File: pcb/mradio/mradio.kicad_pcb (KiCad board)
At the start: 2 copper layers, 150 x 75 mm, 187 parts, among them J202 Conn_01x02, J301 JX0026D21BNL, J401 MM60-52B1-E1-R650, J501 MDT420E01001, U1 STM32H745ZITx, U1001 TPS7A8500ARGRR, U301 DP83825I, U401 74AVC4T774, U402 74AVC4T774, U502 SN74LVC1T45DRL, U601 TPS54560BDDA, U701 TPS54560BDDA, U801 TPS7A8500ARGRR, Y301 DSC1525JL2A-25M00000T

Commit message: started LDO
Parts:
- moved C806 147.6 mm to (28.0, 107.0)
- moved D801 147.6 mm to (36.0, 104.3)
- moved C807 147.6 mm to (32.0, 94.5)
- moved C808 147.6 mm to (32.0, 97.0)
- moved C809 147.6 mm to (32.0, 99.5)
- moved C810 147.6 mm to (32.0, 102.0)
- moved R801 147.6 mm to (32.0, 104.5)
- moved TP801 146.8 mm to (38.8, 96.6)
- moved C804 105.0 mm to (80.2, 93.2), turned to -90 degrees
- moved C805 104.4 mm to (84.5, 91.0)
- moved C803 104.1 mm to (81.2, 90.8)
- moved C802 103.4 mm to (78.8, 93.2), turned to -90 degrees
- moved C801 103.4 mm to (77.2, 93.2), turned to -90 degrees
- moved U801 35.1 mm to (83.2, 93.9), turned to 90 degrees
- moved H401 31.0 mm to (191.1, 78.6)
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
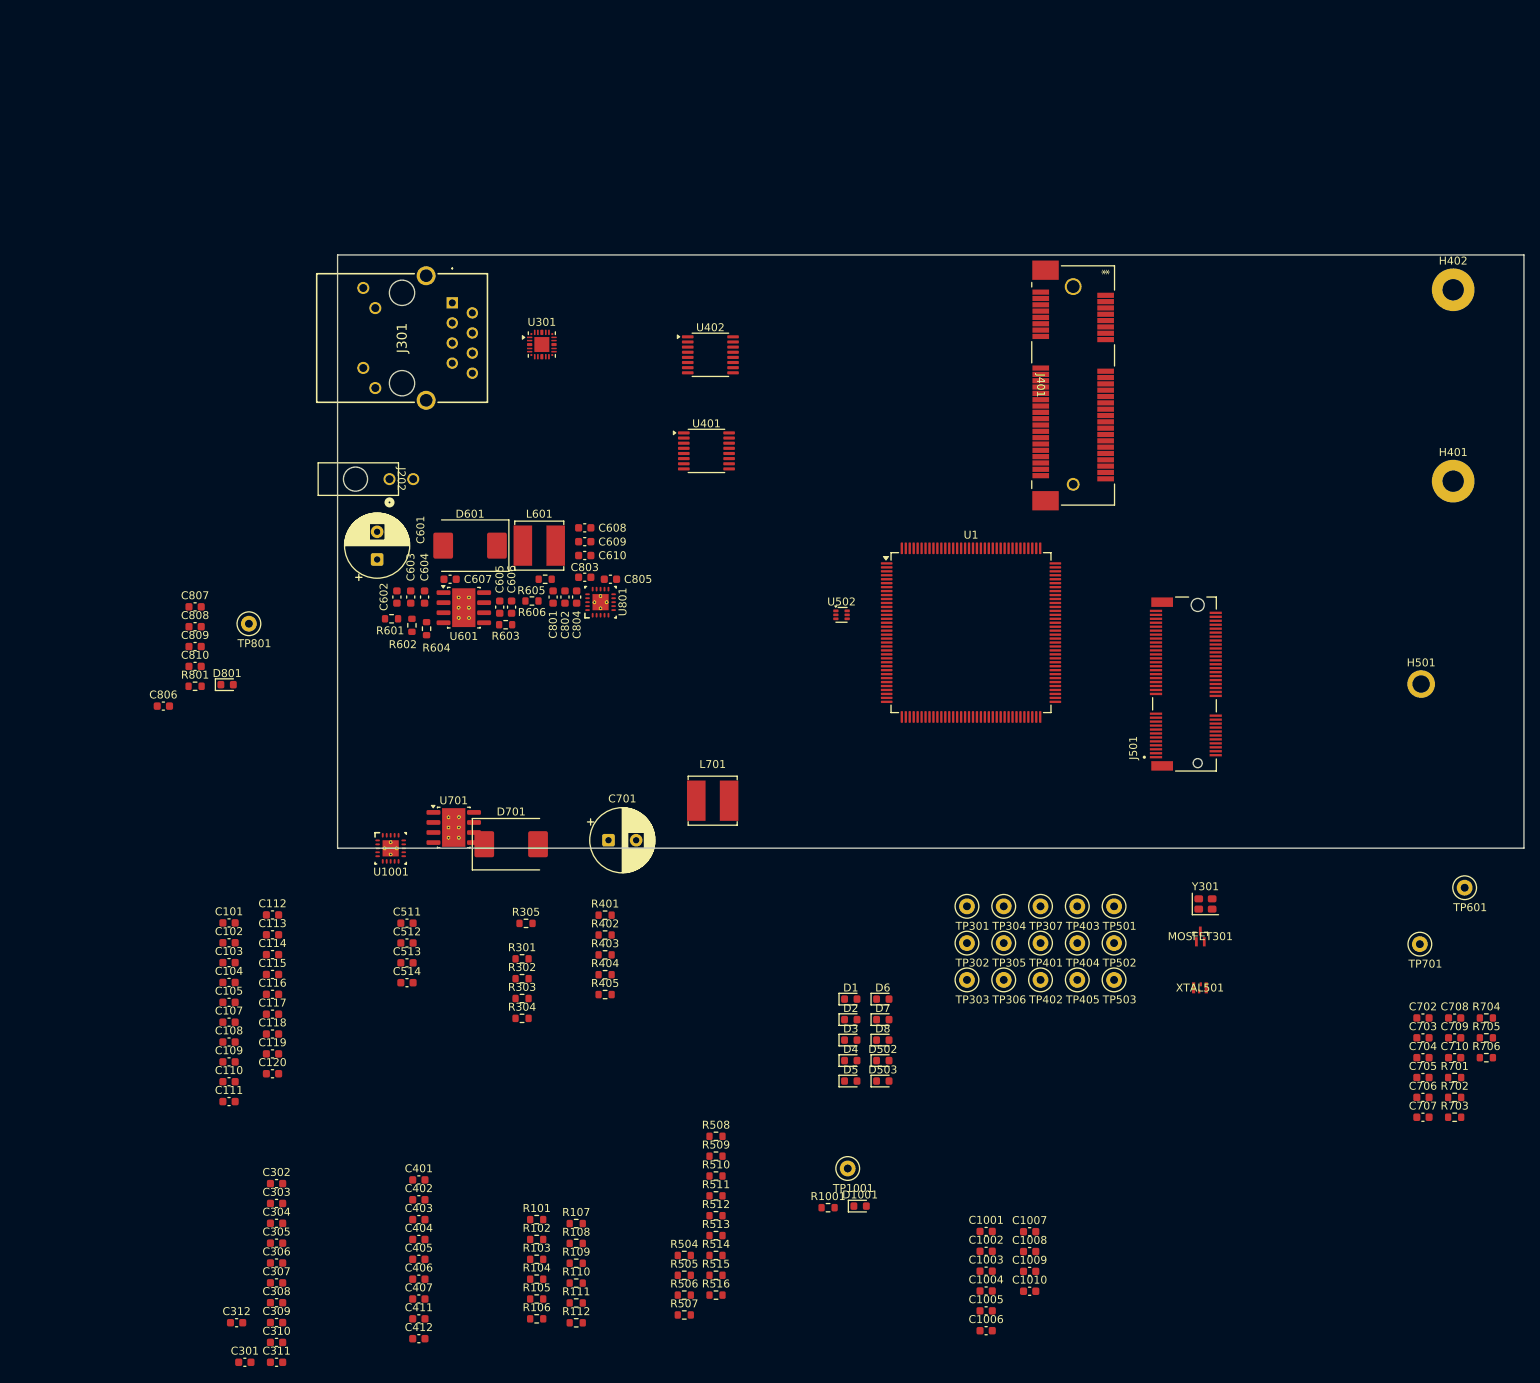
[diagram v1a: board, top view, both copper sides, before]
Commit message: Finished 12->3v3 circuit and 2v2 buck
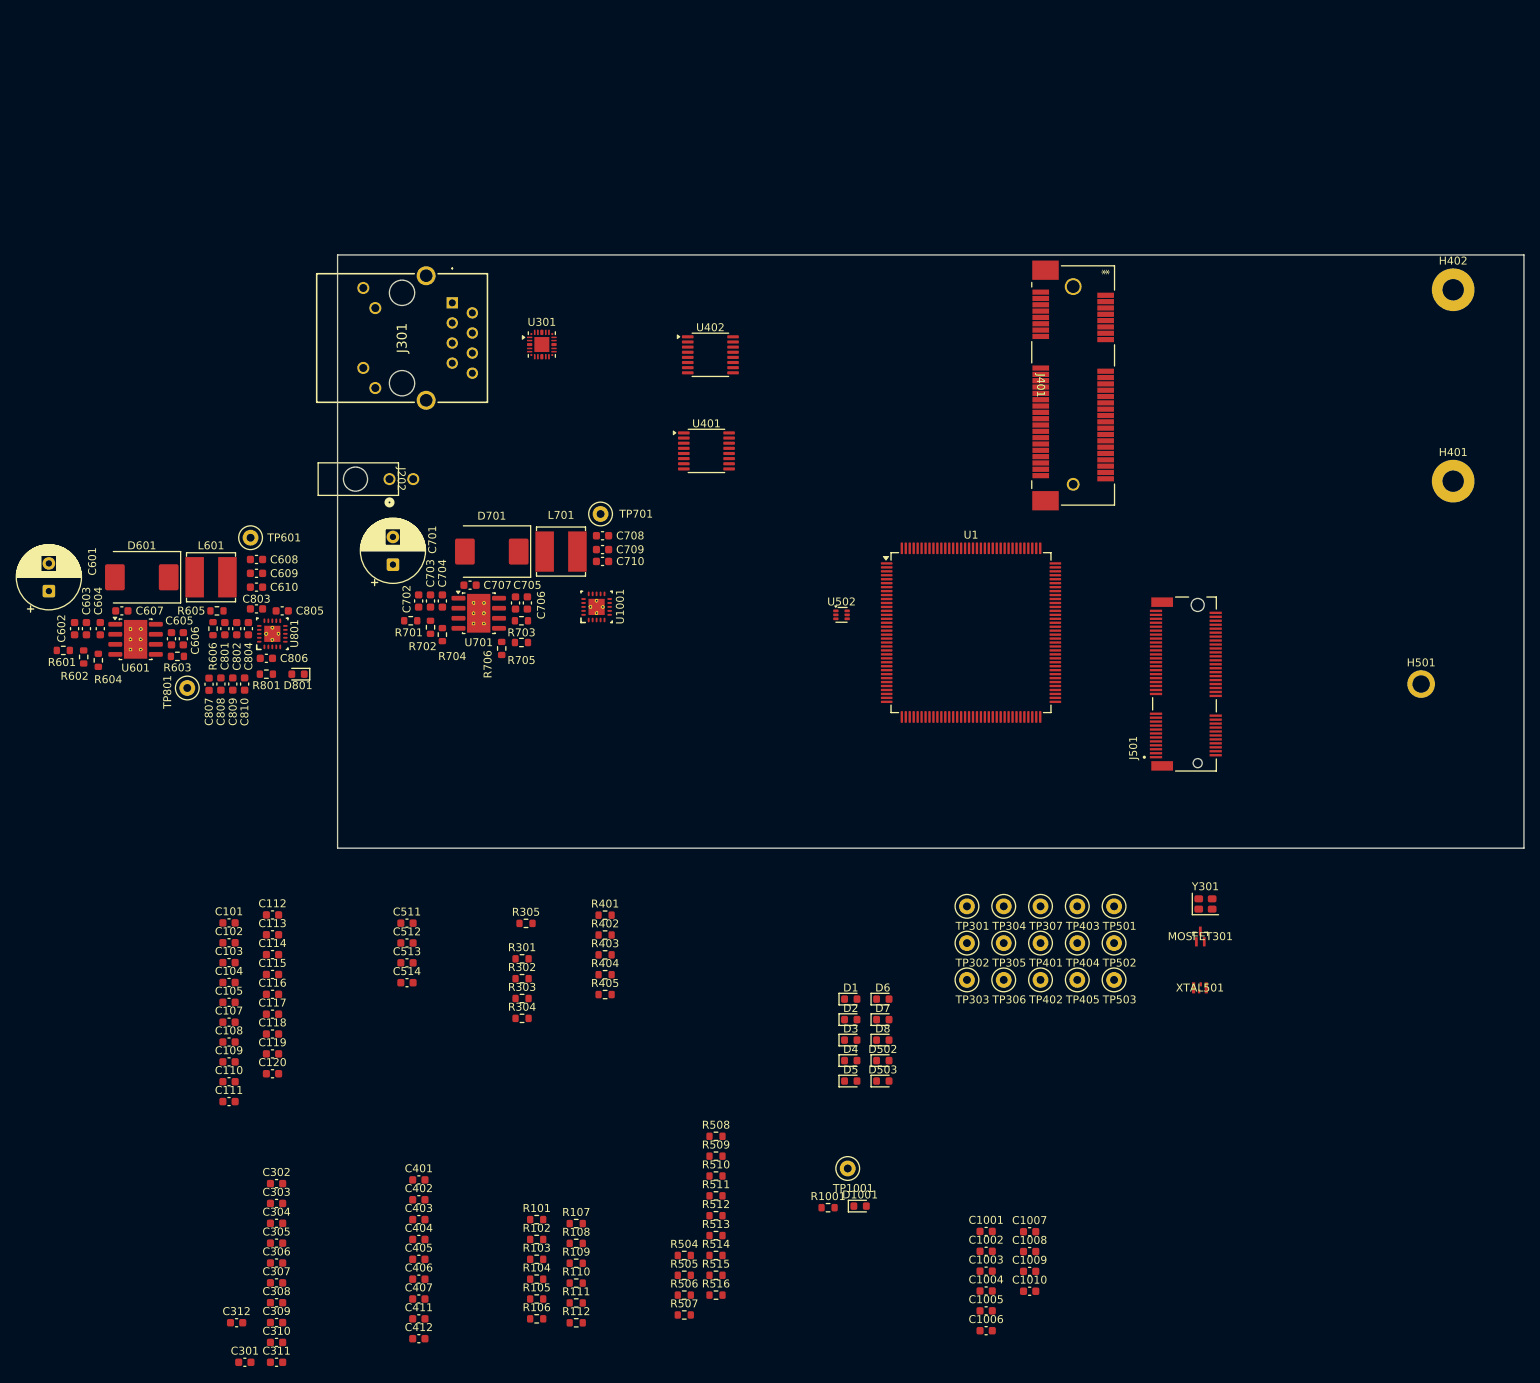
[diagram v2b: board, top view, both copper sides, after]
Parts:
- moved TP601 159.8 mm to (39.0, 85.8)
- moved R701 144.1 mm to (59.2, 96.2)
- moved R702 142.5 mm to (61.8, 97.1), turned to -90 degrees
- moved R704 140.6 mm to (63.2, 98.0), turned to -90 degrees
- moved C707 138.0 mm to (66.8, 91.8)
- moved C702 137.5 mm to (60.2, 93.8), turned to 90 degrees
- moved C703 137.1 mm to (61.8, 93.8), turned to 90 degrees
- moved C704 136.8 mm to (63.2, 93.8), turned to 90 degrees
- moved R706 134.8 mm to (70.8, 99.8), turned to -90 degrees
- moved R703 133.6 mm to (73.2, 96.2), turned to 180 degrees
- moved R705 131.8 mm to (73.2, 99.0), turned to 180 degrees
- moved C705 129.5 mm to (72.5, 94.0), turned to 90 degrees
- moved C706 129.3 mm to (74.0, 94.0), turned to 90 degrees
- moved C710 124.7 mm to (83.5, 88.8)
- moved C709 124.2 mm to (83.5, 87.2)
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
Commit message: power conversion
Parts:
- moved C910 126.6 mm to (41.0, 99.0), turned to 90 degrees
- moved C909 126.2 mm to (39.5, 99.0), turned to 90 degrees
- moved C908 125.8 mm to (38.0, 99.0), turned to 90 degrees
- moved C907 125.5 mm to (36.5, 99.0), turned to 90 degrees
- moved C905 125.2 mm to (44.8, 93.8)
- moved C904 124.5 mm to (41.0, 96.0), turned to -90 degrees
- moved C903 123.8 mm to (41.8, 93.8)
- moved C906 123.6 mm to (43.5, 99.8)
- moved C902 122.3 mm to (39.5, 96.0), turned to -90 degrees
- moved C901 121.8 mm to (38.0, 96.0), turned to -90 degrees
- moved TP901 101.2 mm to (35.2, 102.5)
- moved D901 97.1 mm to (49.2, 99.8), turned to 180 degrees
- moved R901 95.8 mm to (46.5, 100.5), turned to -90 degrees
- moved C601 47.0 mm to (60.5, 92.2)
- moved TP801 46.3 mm to (77.2, 102.5)
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- renumbered C1001 to C901, C1002 to C902, C1003 to C903, C1004 to C904, C1005 to C905, C1006 to C906, C1007 to C907, C1008 to C908, C1009 to C909, C1010 to C910, D1001 to D901, R1001 to R901, TP1001 to TP901, U1001 to U901

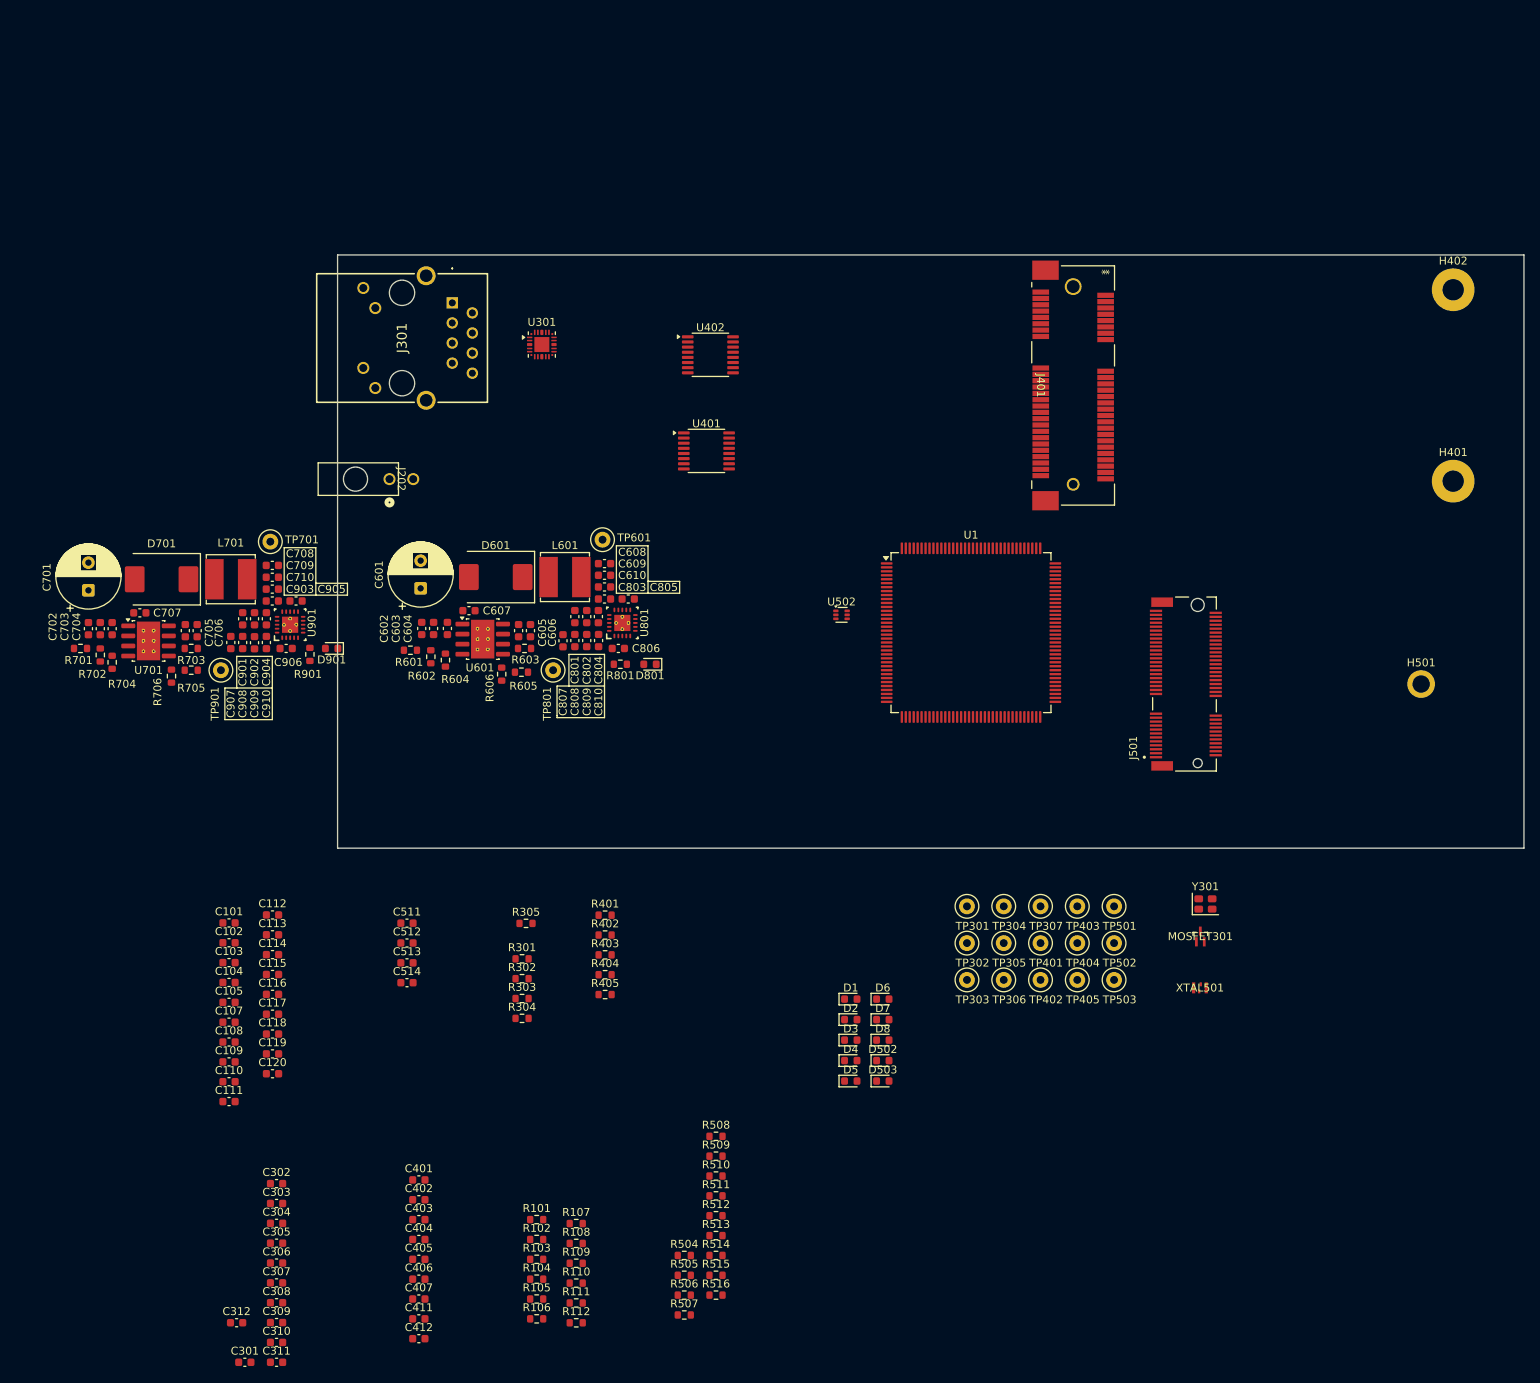
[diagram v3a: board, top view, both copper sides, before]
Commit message: SDIO class and WiFi/mag jack layout
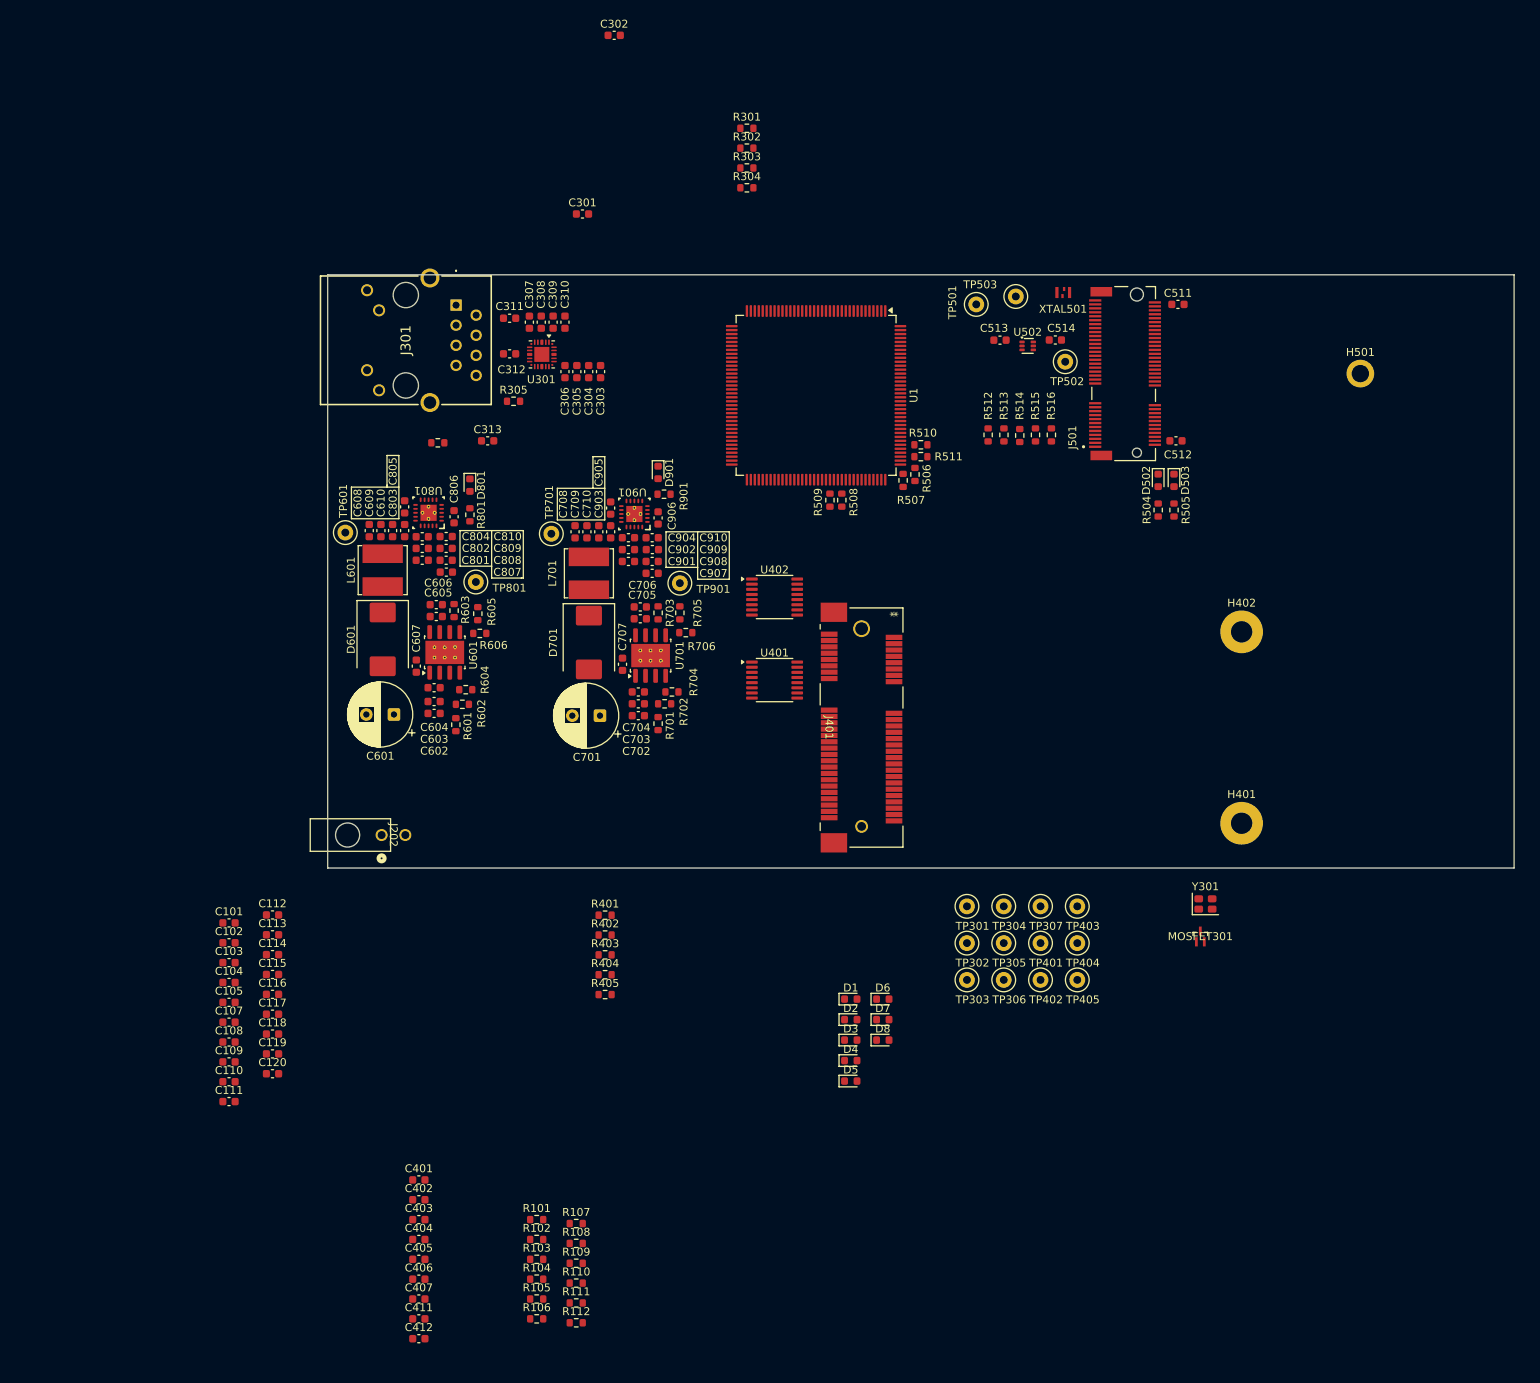
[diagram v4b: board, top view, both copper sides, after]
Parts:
- added C313: 1nF, 1KV, Capacitor_SMD:C_0603_1608Metric, F.Cu at (69.0, 73.5)
- added R306: 1M, Resistor_SMD:R_0603_1608Metric, F.Cu at (62.7, 73.8)
- moved C301 151.3 mm to (81.0, 44.8)
- moved C302 151.3 mm to (85.0, 22.2)
- moved C311 135.2 mm to (71.8, 58.0), turned to 180 degrees
- moved C310 134.0 mm to (78.8, 58.5), turned to -90 degrees
- moved C309 131.2 mm to (77.2, 58.5), turned to -90 degrees
- moved C308 128.4 mm to (75.8, 58.5), turned to -90 degrees
- moved C312 127.3 mm to (71.8, 62.5), turned to 180 degrees
- moved C307 125.6 mm to (74.2, 58.5), turned to -90 degrees
- moved C511 125.0 mm to (156.2, 56.2)
- moved C306 118.5 mm to (78.8, 64.8), turned to 90 degrees
- moved R516 116.7 mm to (140.2, 72.8), turned to 90 degrees
- moved C305 116.5 mm to (80.2, 64.8), turned to 90 degrees
- moved C512 116.1 mm to (156.0, 73.5)
- moved C514 115.4 mm to (140.8, 60.8), turned to 180 degrees
- moved R505 114.9 mm to (155.8, 82.2), turned to 90 degrees
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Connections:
- C107 pad 1: /MCU/VDD_MCU -> +1V8
- C108 pad 1: /MCU/VDD_MCU -> +1V8
- C109 pad 1: /MCU/VDD_MCU -> +1V8
- C110 pad 1: /MCU/VDD_MCU -> +1V8
- C111 pad 1: /MCU/VDD_MCU -> +1V8
- C112 pad 1: /MCU/VDD_MCU -> +1V8
- C113 pad 1: /MCU/VDD_MCU -> +1V8
- C114 pad 1: /MCU/VDD_MCU -> +1V8
- C115 pad 1: /MCU/VDD_MCU -> +1V8
- C116 pad 1: /MCU/VDD_MCU -> +1V8
- C117 pad 1: /MCU/VDD_MCU -> +1V8
- C120 pad 1: /MCU/VDD_MCU -> +1V8
- D1 pad 1: GND -> Net-(D1-K)
- J301 pad 4: GND -> Net-(J301-CHS_GROUND_1)
- J301 pad 5: GND -> Net-(J301-CHS_GROUND_1)
- R102 pad 2: /MCU/VDD_MCU -> +1V8
- R104 pad 2: /MCU/VDD_MCU -> +1V8
- R105 pad 2: /MCU/SoS_LED1 -> +3V3
- U1 pad 105: /MCU/VDD_MCU -> +1V8
- U1 pad 106: Net-(U1-VDD-Pad106) -> +1V8
- U1 pad 119: Net-(U1-VDD-Pad106) -> +1V8
- U1 pad 129: Net-(U1-VDD-Pad106) -> +1V8
- U1 pad 13: Net-(U1-VDD-Pad106) -> +1V8
- U1 pad 143: /MCU/VDD_MCU -> +1V8
- U1 pad 144: Net-(U1-VDD-Pad106) -> +1V8
- U1 pad 16: unconnected-(U1-VDDSMPS-Pad16) -> GND
- U1 pad 17: unconnected-(U1-VFBSMPS-Pad17) -> GND
- U1 pad 19: Net-(U1-VDD-Pad106) -> +1V8
- U1 pad 32: Net-(U1-VDD-Pad106) -> +1V8
- U1 pad 42: Net-(U1-VDD-Pad106) -> +1V8
- U1 pad 56: Net-(U1-VDD-Pad106) -> +1V8
- U1 pad 7: Net-(U1-VDD-Pad106) -> +1V8
- U1 pad 70: /MCU/VDD_MCU -> +1V8
- U1 pad 71: Net-(U1-VDD-Pad106) -> +1V8
- U1 pad 79: Net-(U1-VDD-Pad106) -> +1V8
- U1 pad 8: /MCU/VDD_MCU -> +1V8
- U1 pad 90: /MCU/3v3_LDO_OUT -> +3V3
- U1 pad 91: /MCU/3v3_LDO_OUT -> +3V3
- U1 pad 92: Net-(U1-VDD-Pad106) -> +1V8
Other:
- copper layers 2 -> 4
